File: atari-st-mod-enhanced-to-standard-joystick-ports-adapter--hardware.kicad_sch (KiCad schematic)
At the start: 46 parts, among them J1 Joy0/Mouse, J2 Joy1, J3 Enhanced Joystick Port, J4 OLED 128×64, J5 OLED 128×32, J6 Joy0/Mouse, J7 Joy1, Q1 1<Vgsth<2, Low Rdson, Vds >10, Q10 1<Vgsth<2, Low Rdson, Vds >10, Q2 1<Vgsth<2, Low Rdson, Vds >10, Q3 1<Vgsth<2, Low Rdson, Vds >10, Q4 1<Vgsth<2, Low Rdson, Vds >10, Q5 1<Vgsth<2, Low Rdson, Vds >10, Q6 1<Vgsth<2, Low Rdson, Vds >10, Q7 1<Vgsth<2, Low Rdson, Vds >10, Q8 1<Vgsth<2, Low Rdson, Vds >10, Q9 1<Vgsth<2, Low Rdson, Vds >10, SW1 Selector, SW2 Activate/Change, SW3 Cancel, SW4 Reset, U1 LM4040DBZ-3

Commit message: change selected connector footprint for dsub connectors
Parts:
- J1, J2: footprint Connector_Dsub:DSUB-9_Female_Horizontal_P2.77x2.84mm_EdgePinOffset4.94mm_Housed_MountingHolesOffset7.48mm -> Connector_Dsub:DSUB-9_Female_Horizontal_P2.77x2.84mm_EdgePinOffset7.70mm_Housed_MountingHolesOffset9.12mm
- J3: footprint Connector_Dsub:DSUB-15-HD_Female_Horizontal_P2.29x1.98mm_EdgePinOffset3.03mm_Housed_MountingHolesOffset4.94mm -> Connector_Dsub:DSUB-15-HD_Female_Horizontal_P2.29x1.98mm_EdgePinOffset8.35mm_Housed_MountingHolesOffset10.89mm
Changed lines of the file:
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@@
     (property "Reference" "J1" (id 0) (at 26.67 22.86 0))
     (property "Value" "Joy0/Mouse" (id 1) (at 26.67 48.26 0))
-    (property "Footprint" "Connector_Dsub:DSUB-9_Female_Horizontal_P2.77x2.84mm_EdgePinOffset4.94mm_Housed_MountingHolesOffset7.48mm" (id 2) (at 26.67 35.56 0)
+    (property "Footprint" "Connector_Dsub:DSUB-9_Female_Horizontal_P2.77x2.84mm_EdgePinOffset7.70mm_Housed_MountingHolesOffset9.12mm" (id 2) (at 26.67 35.56 0)
       (effects (font (size 1.27 1.27)) hide)
     )
@@
     (property "Reference" "J3" (id 0) (at 156.21 205.74 0))
     (property "Value" "Enhanced Joystick Port" (id 1) (at 156.21 246.38 0))
-    (property "Footprint" "Connector_Dsub:DSUB-15-HD_Female_Horizontal_P2.29x1.98mm_EdgePinOffset3.03mm_Housed_MountingHolesOffset4.94mm" (id 2) (at 156.21 226.06 0)
+    (property "Footprint" "Connector_Dsub:DSUB-15-HD_Female_Horizontal_P2.29x1.98mm_EdgePinOffset8.35mm_Housed_MountingHolesOffset10.89mm" (id 2) (at 156.21 226.06 0)
       (effects (font (size 1.27 1.27)) hide)
     )
@@
     (property "Reference" "J2" (id 0) (at 74.93 22.86 0))
     (property "Value" "Joy1" (id 1) (at 74.93 48.26 0))
-    (property "Footprint" "Connector_Dsub:DSUB-9_Female_Horizontal_P2.77x2.84mm_EdgePinOffset4.94mm_Housed_MountingHolesOffset7.48mm" (id 2) (at 74.93 35.56 0)
+    (property "Footprint" "Connector_Dsub:DSUB-9_Female_Horizontal_P2.77x2.84mm_EdgePinOffset7.70mm_Housed_MountingHolesOffset9.12mm" (id 2) (at 74.93 35.56 0)
       (effects (font (size 1.27 1.27)) hide)
     )
@@
     )
     (path "/3a41dd27-ec14-44d5-b505-aad1d829f79a"
-      (reference "J1") (unit 1) (value "Joy0/Mouse") (footprint "Connector_Dsub:DSUB-9_Female_Horizontal_P2.77x2.84mm_EdgePinOffset4.94mm_Housed_MountingHolesOffset7.48mm")
+      (reference "J1") (unit 1) (value "Joy0/Mouse") (footprint "Connector_Dsub:DSUB-9_Female_Horizontal_P2.77x2.84mm_EdgePinOffset7.70mm_Housed_MountingHolesOffset9.12mm")
     )
     (path "/4d9a5c15-b6c5-47a2-bb8c-738307f9e339"
-      (reference "J2") (unit 1) (value "Joy1") (footprint "Connector_Dsub:DSUB-9_Female_Horizontal_P2.77x2.84mm_EdgePinOffset4.94mm_Housed_MountingHolesOffset7.48mm")
+      (reference "J2") (unit 1) (value "Joy1") (footprint "Connector_Dsub:DSUB-9_Female_Horizontal_P2.77x2.84mm_EdgePinOffset7.70mm_Housed_MountingHolesOffset9.12mm")
     )
     (path "/413a6d7b-7637-4c53-9629-c2c873aa85eb"
-      (reference "J3") (unit 1) (value "Enhanced Joystick Port") (footprint "Connector_Dsub:DSUB-15-HD_Female_Horizontal_P2.29x1.98mm_EdgePinOffset3.03mm_Housed_MountingHolesOffset4.94mm")
+      (reference "J3") (unit 1) (value "Enhanced Joystick Port") (footprint "Connector_Dsub:DSUB-15-HD_Female_Horizontal_P2.29x1.98mm_EdgePinOffset8.35mm_Housed_MountingHolesOffset10.89mm")
     )
     (path "/87beaccd-9491-499a-bd97-523fb030f5ba"

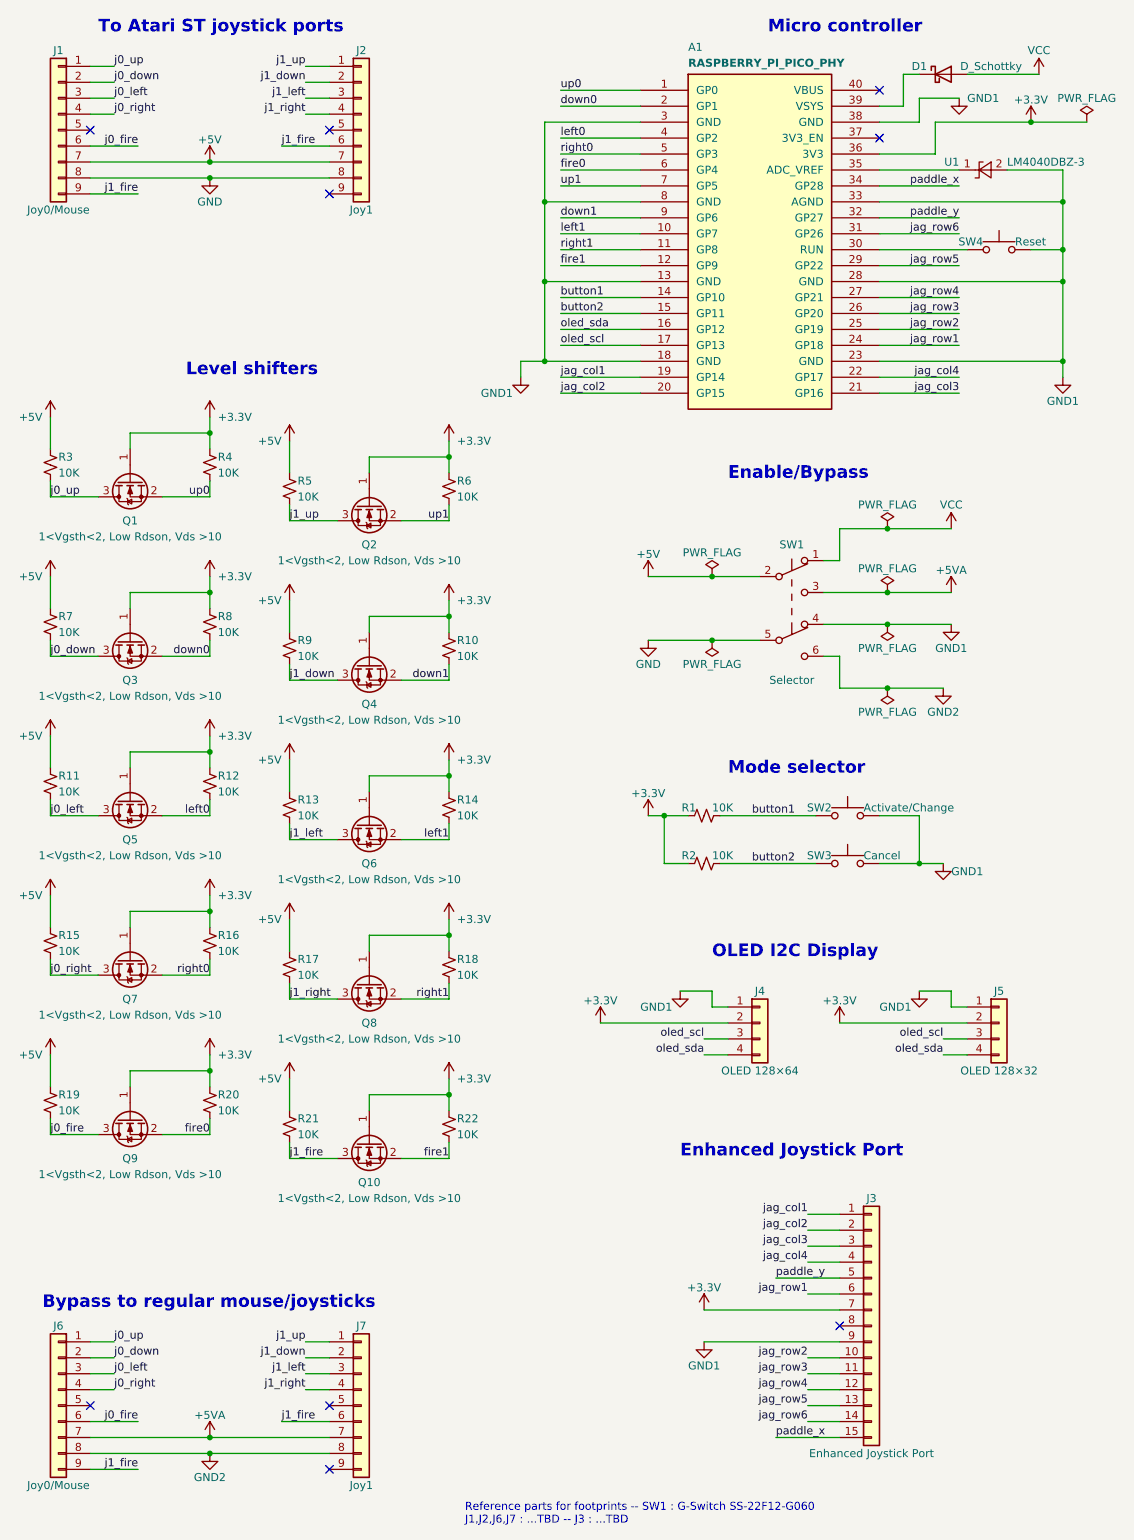
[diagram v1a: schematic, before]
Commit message: rename all components, start adding LCSC parts number
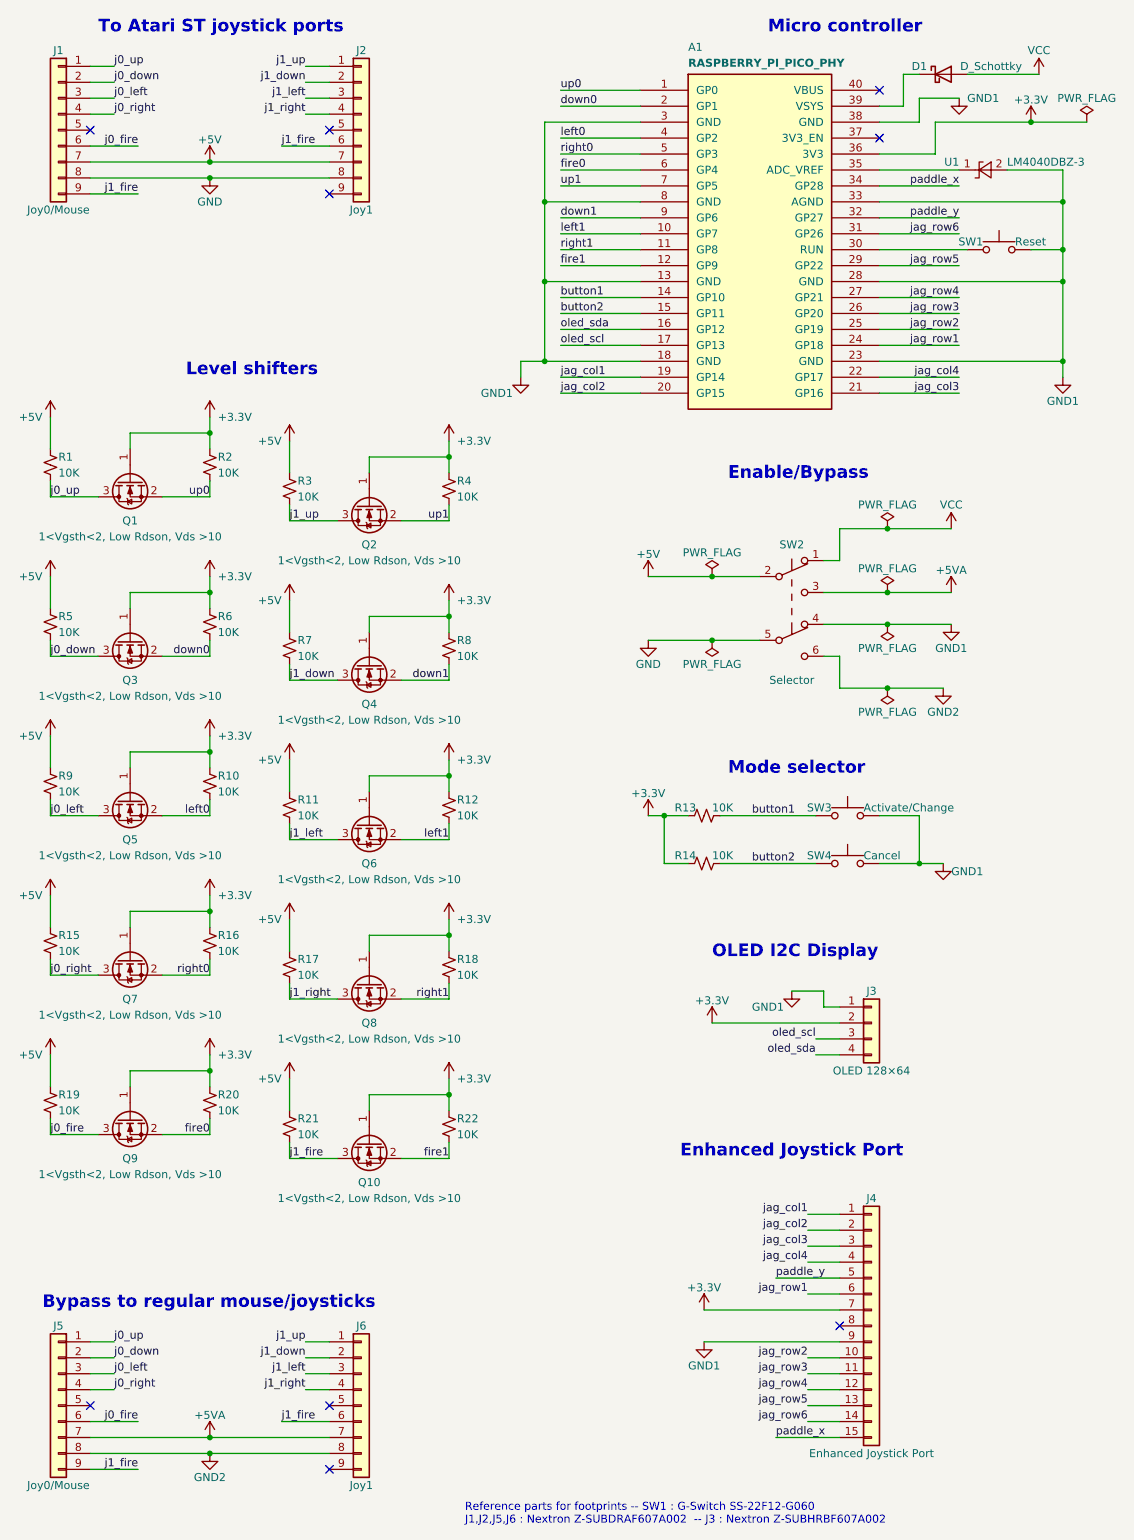
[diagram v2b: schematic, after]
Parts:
- removed J5: OLED 128×32, Connector_PinSocket_2.54mm:PinSocket_1x04_P2.54mm_Vertical, symbol Connector_Generic:Conn_01x04
- J1, J2: LCSC part number (none) -> C115167
- J4: renamed from J3; LCSC part number (none) -> C235848
- J5: renamed from J6; LCSC part number (none) -> C115167
- J6: renamed from J7; LCSC part number (none) -> C115167
- SW2: renamed from SW1; LCSC part number (none) -> C2848906
- renumbered J4 to J3, R3 to R1, R12 to R10, R13 to R11, R14 to R12, R1 to R13, R2 to R14, R4 to R2, R5 to R3, R6 to R4, R7 to R5, R8 to R6, R9 to R7, R10 to R8, R11 to R9, SW4 to SW1, SW2 to SW3, SW3 to SW4
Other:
- note added: "Reference parts for footprints -- SW1 : G-Switch SS-22F12-G060 J1,J2,J5,J6 : Nextron Z-SUBDRAF607A002 -- J3 : Nextron Z-SUBHRBF607A002"
- note removed: "Reference parts for footprints -- SW1 : G-Switch SS-22F12-G060 J1,J2,J6,J7 : ...TBD -- J3 : ...TBD"
- moved on the sheet: J3
